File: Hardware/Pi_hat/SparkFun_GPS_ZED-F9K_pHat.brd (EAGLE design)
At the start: 65 x 56.5 mm, 56 parts, among them J1 QWIIC_RIGHT_ANGLE, J2 RASPBERRYPI-40-PIN-GPIO_PTH_N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, J4 U.FL, U1 UBLOX_ZED_F9K, U3 TRIPLE_BUFFER_74LVC3G07

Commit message: Adds labels to pi hat
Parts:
- added U$11: (no value), bottom labels:INT2
- added U$12: (no value), bottom labels:PPS1
- added U$13: (no value), bottom labels:RESET4
- added U$14: (no value), bottom labels:RXI26
- added U$15: (no value), bottom labels:SAFEBOOT3
- added U$16: (no value), bottom labels:TXO25
- added U$17: (no value), bottom labels:TX_READY0
- added U$18, U$19: (no value), Labels:GND-04
- added U$20: (no value), Labels:I_SUPER2_C-()-04
- added U$21: (no value), even_moar:ANT1
- added U$22: (no value), even_moar:BLK3
- added U$23: (no value), even_moar:GRN2
- added U$24: (no value), even_moar:SPI0
- added U$25: (no value), zed:U#BLOX1
- added U$26: (no value), zed:ZED#F9R0
- added U$27: (no value), NEO_GPS_board_silk_FINAL#03#jpg:NEO_GPS_BOARD_SILK_FINAL#03#JPG
- moved LOGO1 10.9 mm to (18.8, 16.8)
- moved U$5 0.25 mm to (19.8, 3.81)
- moved U$4 0.22 mm to (7.62, 3.81)
- moved U$3 0.17 mm to (14.0, 3.81)
- moved U$7 0.14 mm to (7.35, 27.9)
- moved U$6 0.14 mm to (57.8, 22.6)
- moved U$1 0.13 mm to (7.35, 30.5)
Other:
- board text added: "+"
- board text added: "-"
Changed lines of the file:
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@@
 <setting verticaltext="up"/>
 </settings>
-<grid distance="1" unitdist="mm" unit="mm" style="lines" multiple="1" display="yes" altdistance="0.05" altunitdist="mm" altunit="mm"/>
+<grid distance="1" unitdist="mm" unit="mm" style="lines" multiple="1" display="yes" altdistance="0.5" altunitdist="mm" altunit="mm"/>
 <layers>
 <layer number="1" name="Top" color="4" fill="1" visible="yes" active="yes"/>
 <layer number="2" name="Route2" color="16" fill="1" visible="no" active="no"/>
 <layer number="15" name="Route15" color="23" fill="1" visible="no" active="no"/>
-<layer number="16" name="Bottom" color="31" fill="1" visible="yes" active="yes"/>
-<layer number="17" name="Pads" color="30" fill="1" visible="yes" active="yes"/>
+<layer number="16" name="Bottom" color="3" fill="1" visible="yes" active="yes"/>
+<layer number="17" name="Pads" color="26" fill="1" visible="yes" active="yes"/>
 <layer number="18" name="Vias" color="2" fill="1" visible="yes" active="yes"/>
 <layer number="19" name="Unrouted" color="6" fill="1" visible="yes" active="yes"/>
@@
 <layer number="37" name="tTest" color="7" fill="1" visible="no" active="yes"/>
 <layer number="38" name="bTest" color="7" fill="1" visible="no" active="yes"/>
-<layer number="39" name="tKeepout" color="4" fill="11" visible="yes" active="yes"/>
-<layer number="40" name="bKeepout" color="1" fill="11" visible="yes" active="yes"/>
-<layer number="41" name="tRestrict" color="4" fill="10" visible="yes" active="yes"/>
-<layer number="42" name="bRestrict" color="1" fill="10" visible="yes" active="yes"/>
+<layer number="39" name="tKeepout" color="4" fill="11" visible="no" active="yes"/>
+<layer number="40" name="bKeepout" color="1" fill="11" visible="no" active="yes"/>
+<layer number="41" name="tRestrict" color="4" fill="10" visible="no" active="yes"/>
+<layer number="42" name="bRestrict" color="1" fill="10" visible="no" active="yes"/>
 <layer number="43" name="vRestrict" color="2" fill="10" visible="no" active="yes"/>
 <layer number="44" name="Drills" color="7" fill="1" visible="no" active="yes"/>
@@
 <layer number="115" name="ReferenceISLANDS" color="7" fill="1" visible="no" active="no"/>
 <layer number="116" name="Patch_BOT" color="9" fill="4" visible="no" active="no"/>
-<layer number="117" name="PM_Ref" color="26" fill="1" visible="no" active="yes"/>
+<layer number="117" name="PM_Ref" color="26" fill="1" visible="yes" active="yes"/>
 <layer number="118" name="Rect_Pads" color="7" fill="1" visible="no" active="no"/>
-<layer number="119" name="PF_Ref" color="31" fill="1" visible="no" active="yes"/>
-<layer number="120" name="WFL_Ref" color="25" fill="1" visible="no" active="yes"/>
+<layer number="119" name="PF_Ref" color="31" fill="1" visible="yes" active="yes"/>
+<layer number="120" name="WFL_Ref" color="25" fill="1" visible="yes" active="yes"/>
 <layer number="121" name="_tsilk" color="7" fill="1" visible="no" active="no"/>
 <layer number="122" name="_bsilk" color="7" fill="1" visible="no" active="no"/>
@@
 <circle x="61.5" y="52.5" radius="3.1" width="0" layer="41"/>
 <circle x="61.5" y="52.5" radius="3.1" width="0" layer="42"/>
+<text x="56.261" y="47.625" size="1.778" layer="21" font="vector" ratio="15">+</text>
+<text x="52.832" y="47.498" size="1.778" layer="21" font="vector" ratio="15">-</text>
 </plain>
 <attributes>
@@
 <attribute name="VALUE" x="65.032" y="13.73" size="0.6096" layer="27" font="vector" ratio="20" rot="R90"/>
 </element>
-<element name="U$1" library="ALL_LABELS" package="INT1" value="" x="7.35" y="30.35" smashed="yes"/>
-<element name="U$2" library="ALL_LABELS" package="PPS4" value="" x="7.35" y="22.75" smashed="yes"/>
-<element name="U$3" library="ALL_LABELS" package="PPS6" value="" x="13.8" y="3.8" smashed="yes"/>
-<element name="U$4" library="ALL_LABELS" package="PWR7" value="" x="7.4" y="3.85" smashed="yes"/>
-<element name="U$5" library="ALL_LABELS" package="RTK5" value="" x="19.6" y="3.95" smashed="yes"/>
-<element name="U$6" library="ALL_LABELS" package="RXI28" value="" x="57.65" y="22.55" smashed="yes"/>
-<element name="U$7" library="ALL_LABELS" package="SAFEBOOT2" value="" x="7.35" y="27.8" smashed="yes"/>
-<element name="U$9" library="ALL_LABELS" package="TX_READY0" value="" x="7.35" y="33" smashed="yes"/>
-<element name="U$8" library="moar" package="RESET0" value="" x="7.35" y="25.3" smashed="yes"/>
-<element name="U$10" library="moar" package="TXO21" value="" x="56.85" y="25.1" smashed="yes"/>
-<element name="LOGO1" library="SparkFun-Aesthetics" package="SFE_LOGO_NAME_FLAME_.2" value="SFE_LOGO_NAME_FLAME.2_INCH" x="29" y="13" smashed="yes"/>
+<element name="U$1" library="ALL_LABELS" package="INT1" value="" x="7.35" y="30.48" smashed="yes"/>
+<element name="U$2" library="ALL_LABELS" package="PPS4" value="" x="7.35" y="22.733" smashed="yes"/>
+<element name="U$3" library="ALL_LABELS" package="PPS6" value="" x="13.97" y="3.81" smashed="yes"/>
+<element name="U$4" library="ALL_LABELS" package="PWR7" value="" x="7.62" y="3.81" smashed="yes"/>
+<element name="U$5" library="ALL_LABELS" package="RTK5" value="" x="19.812" y="3.81" smashed="yes"/>
+<element name="U$6" library="ALL_LABELS" package="RXI28" value="" x="57.777" y="22.606" smashed="yes"/>
+<element name="U$7" library="ALL_LABELS" package="SAFEBOOT2" value="" x="7.35" y="27.94" smashed="yes"/>
+<element name="U$9" library="ALL_LABELS" package="TX_READY0" value="" x="7.35" y="33.02" smashed="yes"/>
+<element name="U$8" library="moar" package="RESET0" value="" x="7.35" y="25.273" smashed="yes"/>
+<element name="U$10" library="moar" package="TXO21" value="" x="56.85" y="25.146" smashed="yes"/>
+<element name="LOGO1" library="SparkFun-Aesthetics" package="SFE_LOGO_NAME_FLAME_.2" value="SFE_LOGO_NAME_FLAME.2_INCH" x="18.84" y="16.81" smashed="yes"/>
 <element name="LOGO2" library="SparkFun-Aesthetics" package="OSHW-LOGO-M" value="OSHW-LOGOM" x="4" y="12" smashed="yes"/>
 <element name="LOGO3" library="SparkFun-Aesthetics" package="QWIIC_5MM" value="QWIIC_LOGO_5MM" x="3" y="47" smashed="yes"/>
+<element name="U$11" library="bottom labels" package="INT2" value="" x="11.557" y="30.48" smashed="yes" rot="MR0"/>
+<element name="U$12" library="bottom labels" package="PPS1" value="" x="11.811" y="22.733" smashed="yes" rot="MR0"/>
+<element name="U$13" library="bottom labels" package="RESET4" value="" x="13.716" y="25.273" smashed="yes" rot="MR0"/>
+<element name="U$14" library="bottom labels" package="RXI26" value="" x="62.738" y="22.606" smashed="yes" rot="MR0"/>
+<element name="U$15" library="bottom labels" package="SAFEBOOT3" value="" x="17.018" y="27.94" smashed="yes" rot="MR0"/>
+<element name="U$16" library="bottom labels" package="TXO25" value="" x="62.738" y="25.146" smashed="yes" rot="MR0"/>
+<element name="U$17" library="bottom labels" package="TX_READY0" value="" x="16.51" y="33.02" smashed="yes" rot="MR0"/>
+<element name="U$18" library="Labels" package="GND-04" value="" x="57.912" y="14.986" smashed="yes"/>
+<element name="U$19" library="Labels" package="GND-04" value="" x="62.738" y="14.986" smashed="yes" rot="MR0"/>
+<element name="U$20" library="Labels" package="I_SUPER2_C-()-04" value="" x="12.954" y="38.354" smashed="yes" rot="MR0"/>
+<element name="U$21" library="even_moar" package="ANT1" value="" x="26.416" y="3.81" smashed="yes"/>
+<element name="U$22" library="even_moar" package="BLK3" value="" x="60.706" y="12.7" smashed="yes"/>
+<element name="U$23" library="even_moar" package="GRN2" value="" x="60.579" y="29.464" smashed="yes"/>
+<element name="U$24" library="even_moar" package="SPI0" value="" x="20.955" y="32.131" smashed="yes" rot="MR0"/>
+<element name="U$25" library="zed" package="U#BLOX1" value="" x="10.16" y="12.7" smashed="yes"/>
+<element name="U$26" library="zed" package="ZED#F9R0" value="" x="8.001" y="8.89" smashed="yes"/>
+<element name="U$27" library="NEO_GPS_board_silk_FINAL#03#jpg" package="NEO_GPS_BOARD_SILK_FINAL#03#JPG" value="" x="32.766" y="13.208" smashed="yes"/>
 </elements>
 <signals>

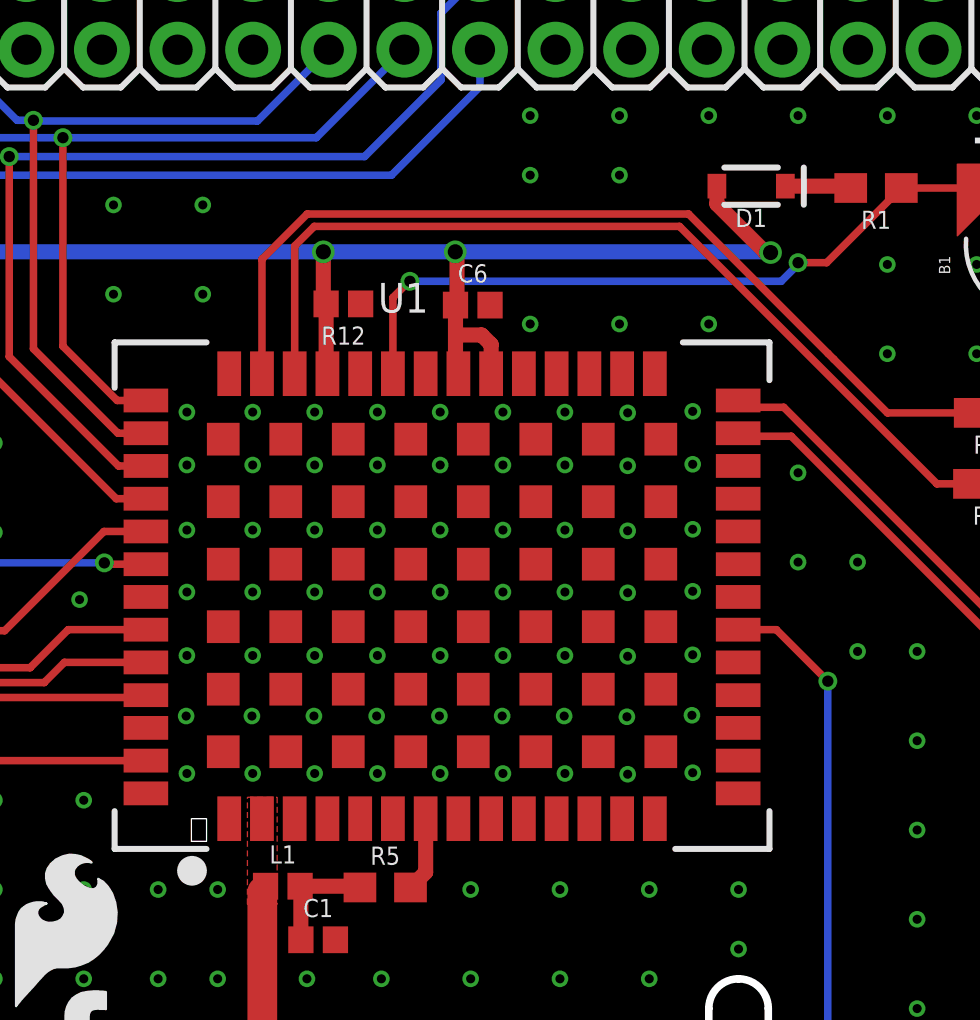
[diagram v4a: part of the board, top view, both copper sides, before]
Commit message: Adds labels to the pi-hat
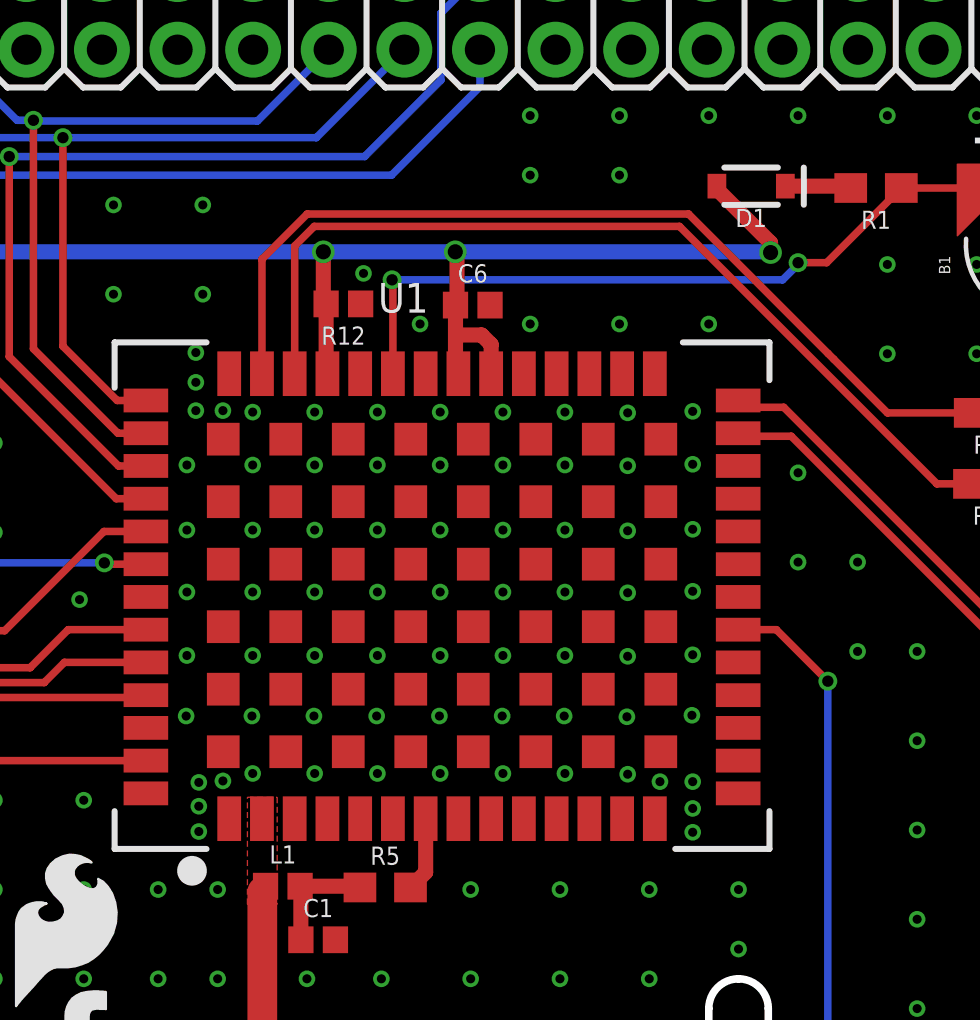
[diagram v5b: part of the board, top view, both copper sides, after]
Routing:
- net GND: vias 271 -> 282
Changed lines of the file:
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@@
 <setting verticaltext="up"/>
 </settings>
-<grid distance="1" unitdist="mm" unit="mm" style="lines" multiple="1" display="yes" altdistance="0.5" altunitdist="mm" altunit="mm"/>
+<grid distance="1" unitdist="mm" unit="mm" style="lines" multiple="1" display="yes" altdistance="0.05" altunitdist="mm" altunit="mm"/>
 <layers>
 <layer number="1" name="Top" color="4" fill="1" visible="yes" active="yes"/>
@@
 <contactref element="J2" pad="30"/>
 <contactref element="J2" pad="14"/>
-<via x="26.4668" y="39.0398" extent="1-16" drill="0.3048"/>
+<via x="26.7668" y="39.0898" extent="1-16" drill="0.3048"/>
 <via x="28.6766" y="39.0398" extent="1-16" drill="0.3048"/>
 <via x="30.7594" y="39.0398" extent="1-16" drill="0.3048"/>
@@
 <via x="41.2496" y="28.8036" extent="1-16" drill="0.3048"/>
 <via x="43.434" y="28.8544" extent="1-16" drill="0.3048"/>
-<via x="26.4668" y="26.8986" extent="1-16" drill="0.3048"/>
+<via x="26.8668" y="26.5986" extent="1-16" drill="0.3048"/>
 <via x="28.6766" y="26.8986" extent="1-16" drill="0.3048"/>
 <via x="30.7594" y="26.8986" extent="1-16" drill="0.3048"/>
@@
 <via x="39.1668" y="26.8986" extent="1-16" drill="0.3048"/>
 <via x="41.275" y="26.8732" extent="1-16" drill="0.3048"/>
-<via x="43.4594" y="26.924" extent="1-16" drill="0.3048"/>
+<via x="43.4594" y="26.624" extent="1-16" drill="0.3048"/>
 <contactref element="J1" pad="1"/>
 <via x="22.86" y="32.7406" extent="1-16" drill="0.3048"/>
@@
 <via x="3" y="44" extent="1-16" drill="0.3048"/>
 <via x="3" y="41" extent="1-16" drill="0.3048"/>
+<via x="32.4" y="43.7" extent="1-16" drill="0.3048"/>
+<via x="34.3" y="42" extent="1-16" drill="0.3048"/>
+<via x="43.4594" y="25.724" extent="1-16" drill="0.3048"/>
+<via x="43.4594" y="24.924" extent="1-16" drill="0.3048"/>
+<via x="26.8668" y="25.7986" extent="1-16" drill="0.3048"/>
+<via x="26.8668" y="24.9486" extent="1-16" drill="0.3048"/>
+<via x="26.7668" y="40.0398" extent="1-16" drill="0.3048"/>
+<via x="26.7668" y="41.0398" extent="1-16" drill="0.3048"/>
+<via x="27.6766" y="39.0898" extent="1-16" drill="0.3048"/>
+<via x="27.6766" y="26.6486" extent="1-16" drill="0.3048"/>
+<via x="42.3594" y="26.624" extent="1-16" drill="0.3048"/>
 </signal>
 <signal name="3.3V">
@@
 <wire x1="11" y1="33" x2="11" y2="40.408" width="0.254" layer="16"/>
 <wire x1="13.4786" y1="30.5214" x2="11" y2="33" width="0.254" layer="16"/>
-<wire x1="46.0762" y1="44.3998" x2="45.904" y2="44.3998" width="0.508" layer="1"/>
-<wire x1="45.904" y1="44.3998" x2="44.2726" y2="46.0312" width="0.508" layer="1"/>
-<wire x1="44.2726" y1="46.0312" x2="44.2726" y2="46.6312" width="0.508" layer="1"/>
+<wire x1="46.0762" y1="44.3998" x2="46.0762" y2="44.7276" width="0.508" layer="1"/>
+<wire x1="46.0762" y1="44.7276" x2="44.2726" y2="46.5312" width="0.508" layer="1"/>
+<wire x1="44.2726" y1="46.5312" x2="44.2726" y2="46.6312" width="0.508" layer="1"/>
 <wire x1="9.123" y1="2" x2="9.123" y2="3.123" width="0.254" layer="1"/>
 <wire x1="13.4786" y1="29.252" x2="13.4732" y2="29.2466" width="0.254" layer="16"/>
@@
 <contactref element="B1" pad="+"/>
 <contactref element="U1" pad="P36"/>
-<wire x1="33.388" y1="40.33" x2="33.388" y2="42.8876" width="0.254" layer="1"/>
-<wire x1="33.388" y1="42.8876" x2="33.9344" y2="43.434" width="0.254" layer="1"/>
-<wire x1="33.9344" y1="43.434" x2="33.9598" y2="43.434" width="0.254" layer="1"/>
-<via x="33.9598" y="43.434" extent="1-16" drill="0.381"/>
-<wire x1="33.9598" y1="43.434" x2="46.434" y2="43.434" width="0.254" layer="16"/>
+<wire x1="33.3598" y1="43.484" x2="33.388" y2="43.4558" width="0.254" layer="1"/>
+<wire x1="33.388" y1="43.4558" x2="33.388" y2="40.33" width="0.254" layer="1"/>
+<via x="33.3598" y="43.484" extent="1-16" drill="0.381"/>
+<wire x1="33.3598" y1="43.484" x2="46.484" y2="43.484" width="0.254" layer="16"/>
 <via x="47" y="44.0602" extent="1-16" drill="0.381"/>
-<wire x1="46.434" y1="43.434" x2="47" y2="44" width="0.254" layer="16"/>
+<wire x1="46.484" y1="43.484" x2="47" y2="44" width="0.254" layer="16"/>
 <wire x1="47" y1="44" x2="47" y2="44.0602" width="0.254" layer="16"/>
 <wire x1="47" y1="44.0602" x2="47.9608" y2="44.0602" width="0.254" layer="1"/>
